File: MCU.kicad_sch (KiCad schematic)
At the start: 17 parts, among them J1 Conn_ARM_SWD_TagConnect_TC203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, U1 MCU_0001, Y1 CLK_0001

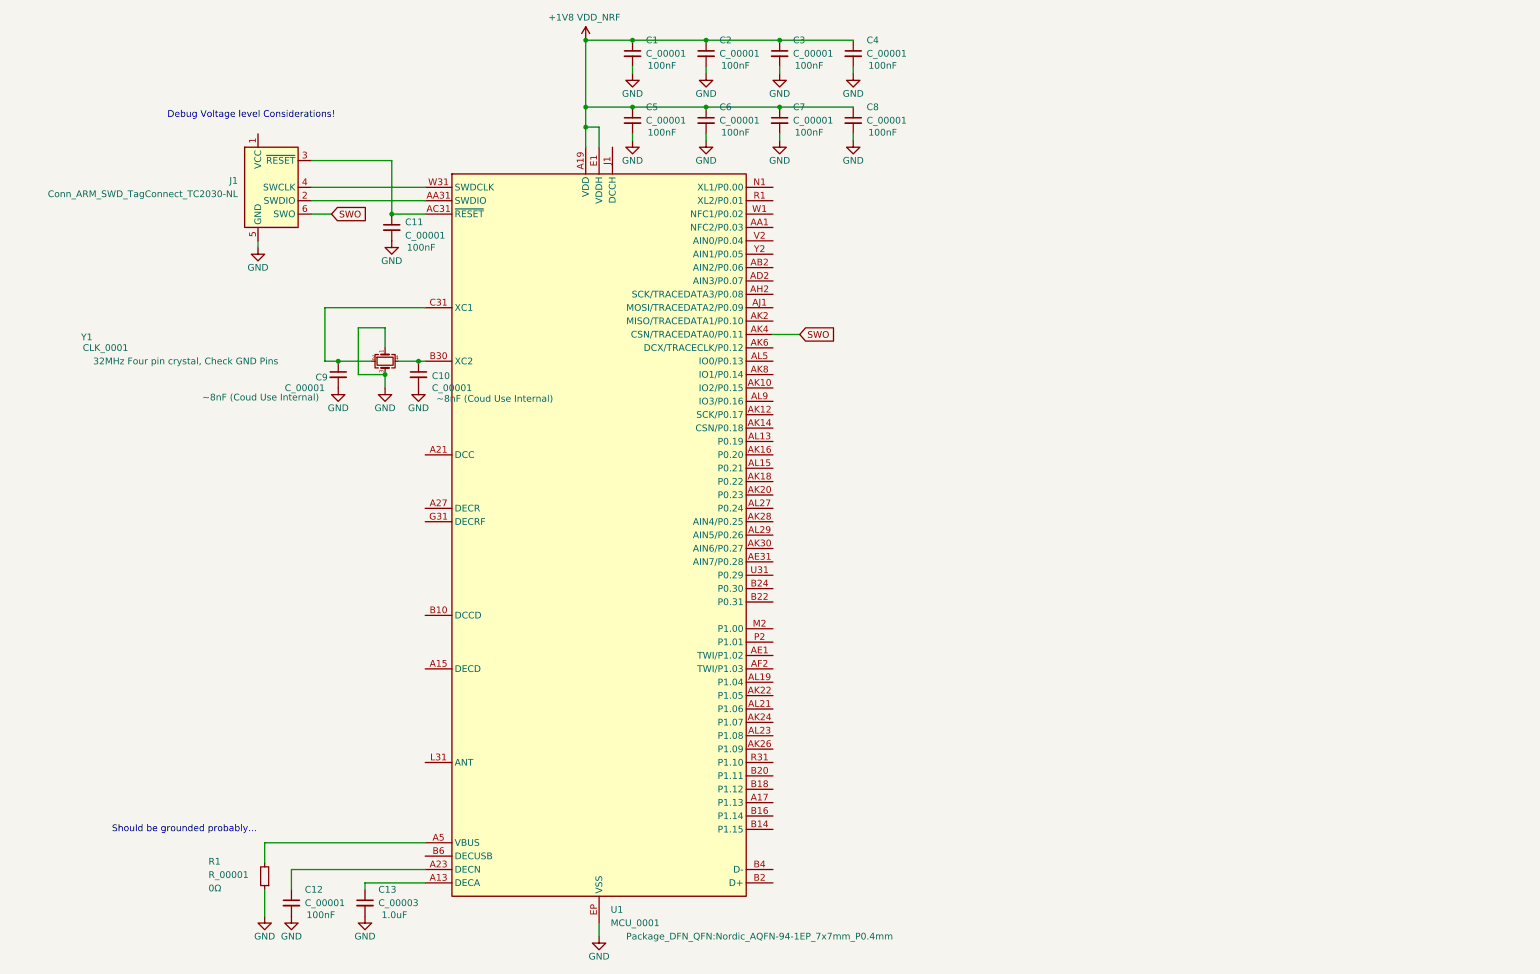
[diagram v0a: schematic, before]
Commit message: added inductors for DCDC regulators
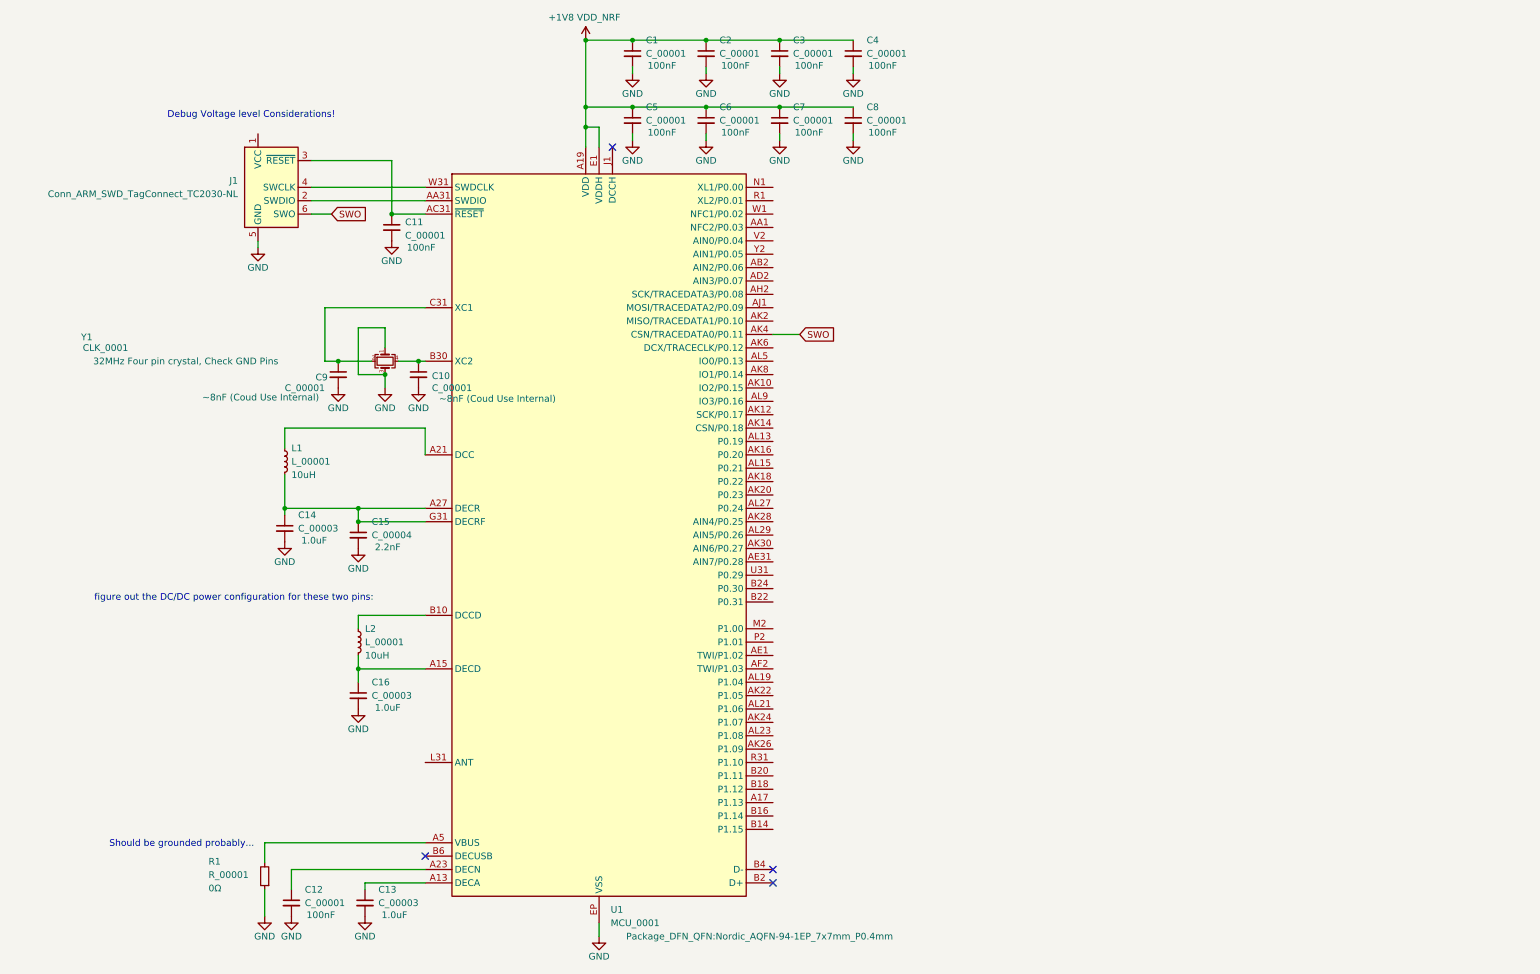
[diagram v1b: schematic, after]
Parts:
- added C14, C16: C_00003, symbol mic_patch_parts:C_00003
- added C15: C_00004, symbol mic_patch_parts:C_00004
- added L1, L2: L_00001, symbol mic_patch_parts:L_00001
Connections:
- net GND: now also C14.2, C15.2, C16.2
- net at U1.A15 (DECD): now also C16.1, L2.2
- net at U1.A21 (DCC): now also L1.1
- net at U1.A27 (DECR): now also U1.G31 (DECRF), C14.1, C15.1, L1.2
- net at U1.B10 (DCCD): now also L2.1
- no-connect marks 0 -> 4
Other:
- note added: "figure out the DC/DC power configuration for these two pins:"

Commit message: routed power
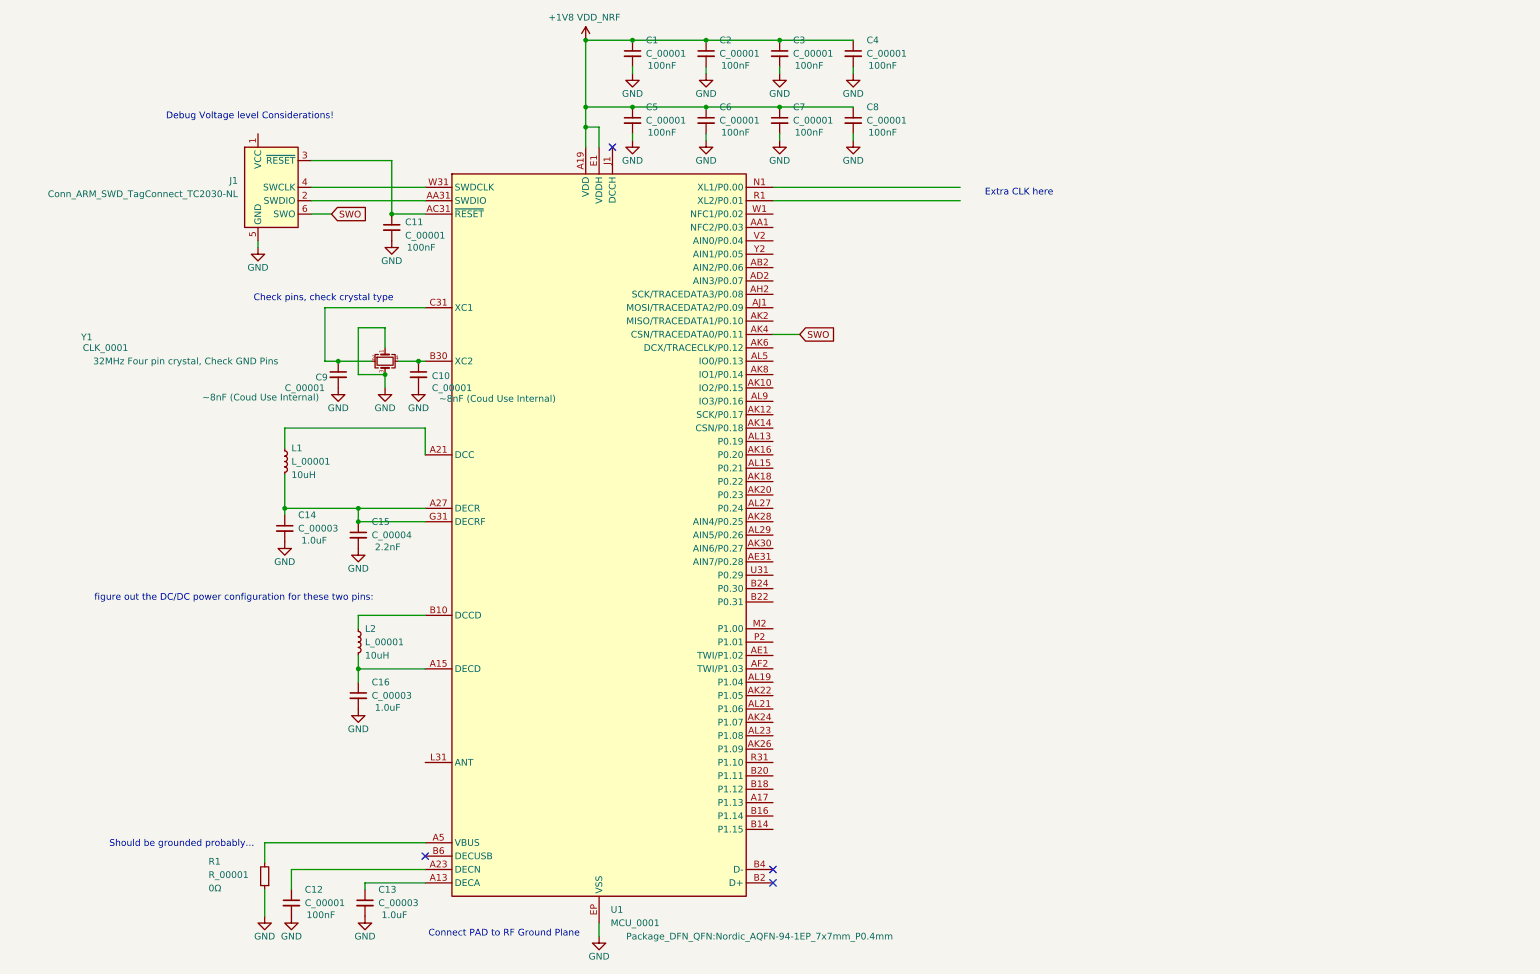
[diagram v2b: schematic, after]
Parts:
- R1: LCSC PNs C11702 -> (none); MPNs 0402WGF1001TCE -> (none)
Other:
- note added: "Check pins, check crystal type"
- note added: "Connect PAD to RF Ground Plane"
- note added: "Extra CLK here"
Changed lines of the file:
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@@
+	(wire
+		(pts
+			(xy 144.78 48.26) (xy 180.34 48.26)
+		)
+		(stroke
+			(width 0)
+			(type default)
+		)
+	)
 	(wire
 		(pts
@@
 	(wire
 		(pts
+			(xy 144.78 50.8) (xy 180.34 50.8)
+		)
+		(stroke
+			(width 0)
+			(type default)
+		)
+	)
+	(wire
+		(pts
 			(xy 66.04 74.93) (xy 71.12 74.93)
 		)
@@
 			(width 0)
 			(type default)
+		)
+	)
+	(text "Extra CLK here"
+		(exclude_from_sim no)
+		(at 191.516 49.276 0)
+		(effects
+			(font
+				(size 1.27 1.27)
+			)
+		)
+	)
+	(text "Connect PAD to RF Ground Plane"
+		(exclude_from_sim no)
+		(at 93.726 189.992 0)
+		(effects
+			(font
+				(size 1.27 1.27)
+			)
 		)
 	)
@@
 		)
 	)
+	(text "Check pins, check crystal type"
+		(exclude_from_sim no)
+		(at 59.436 69.342 0)
+		(effects
+			(font
+				(size 1.27 1.27)
+			)
+		)
+	)
 	(text "Should be grounded probably..."
 		(exclude_from_sim no)
@@
 	(text "Debug Voltage level Considerations!"
 		(exclude_from_sim no)
-		(at 45.72 34.544 0)
+		(at 45.466 34.798 0)
 		(effects
 			(font
@@
 			)
 		)
-		(property "MPNs" "0402WGF1001TCE"
+		(property "MPNs" ""
 			(at 48.26 179.07 0)
 			(effects
@@
 			)
 		)
-		(property "LCSC PNs" "C11702"
+		(property "LCSC PNs" ""
 			(at 48.26 179.07 0)
 			(effects

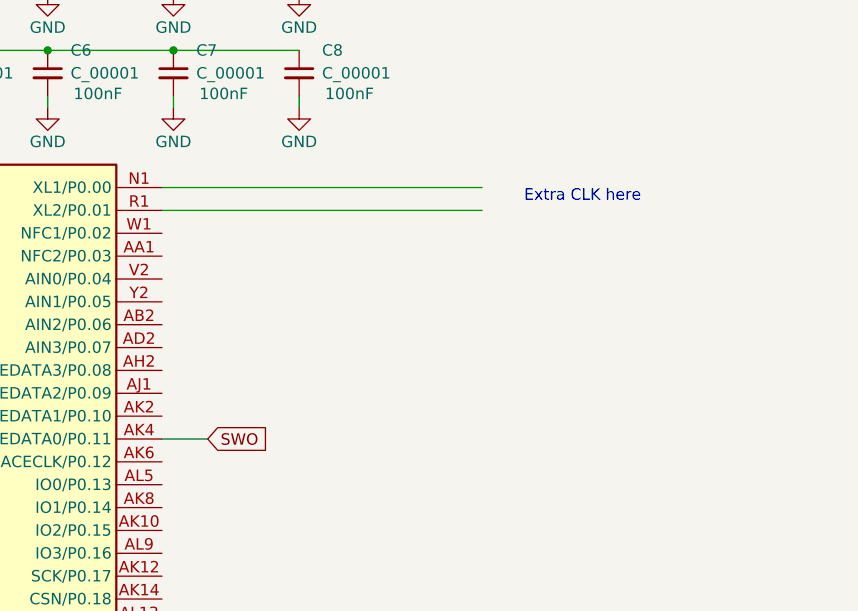
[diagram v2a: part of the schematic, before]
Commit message: added in LFCLK
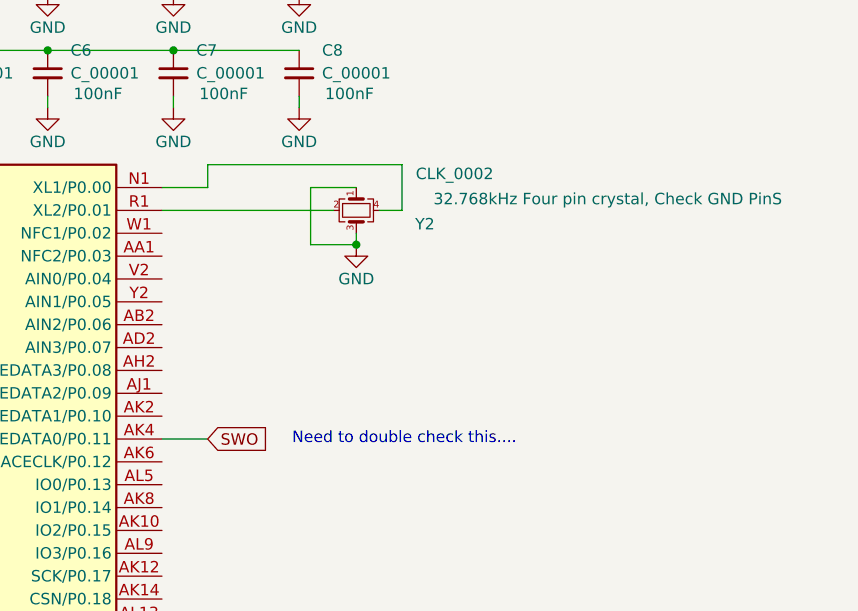
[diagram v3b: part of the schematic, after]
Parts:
- added Y2: CLK_0002, symbol mic_patch_parts:CLK_0002
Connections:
- net GND: now also Y2.1, Y2.3
- net at U1.N1 (XL1/P0.00): now also Y2.4
- net at U1.R1 (XL2/P0.01): now also Y2.2
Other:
- note added: "Need to double check this...."
- note removed: "Extra CLK here"

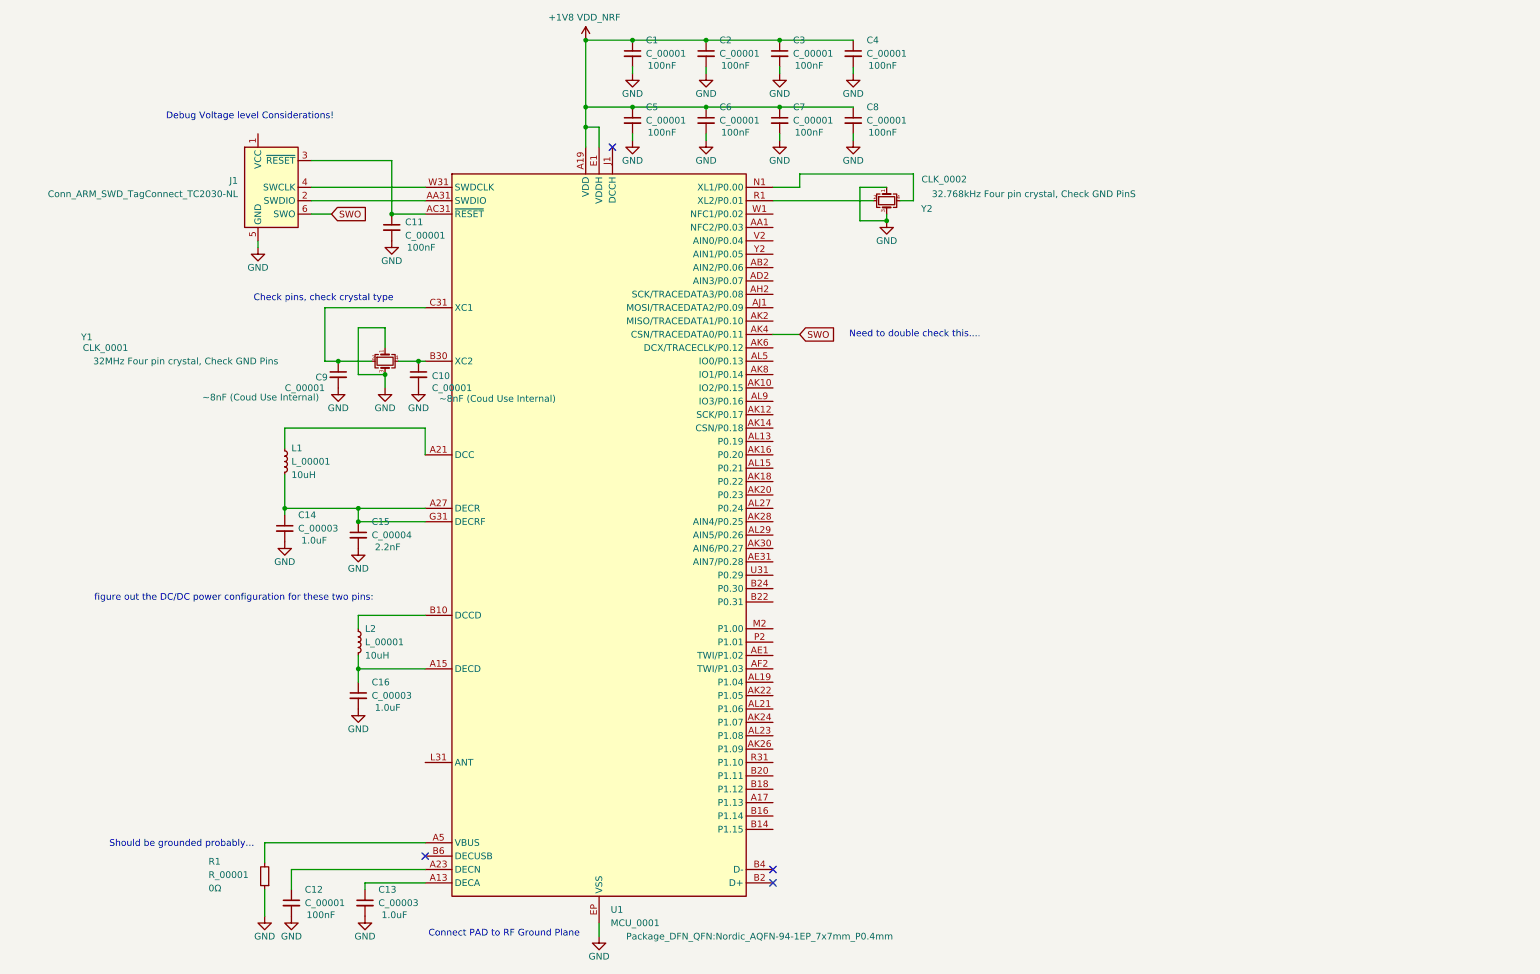
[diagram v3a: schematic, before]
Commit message: added ADAU7002 Symbol
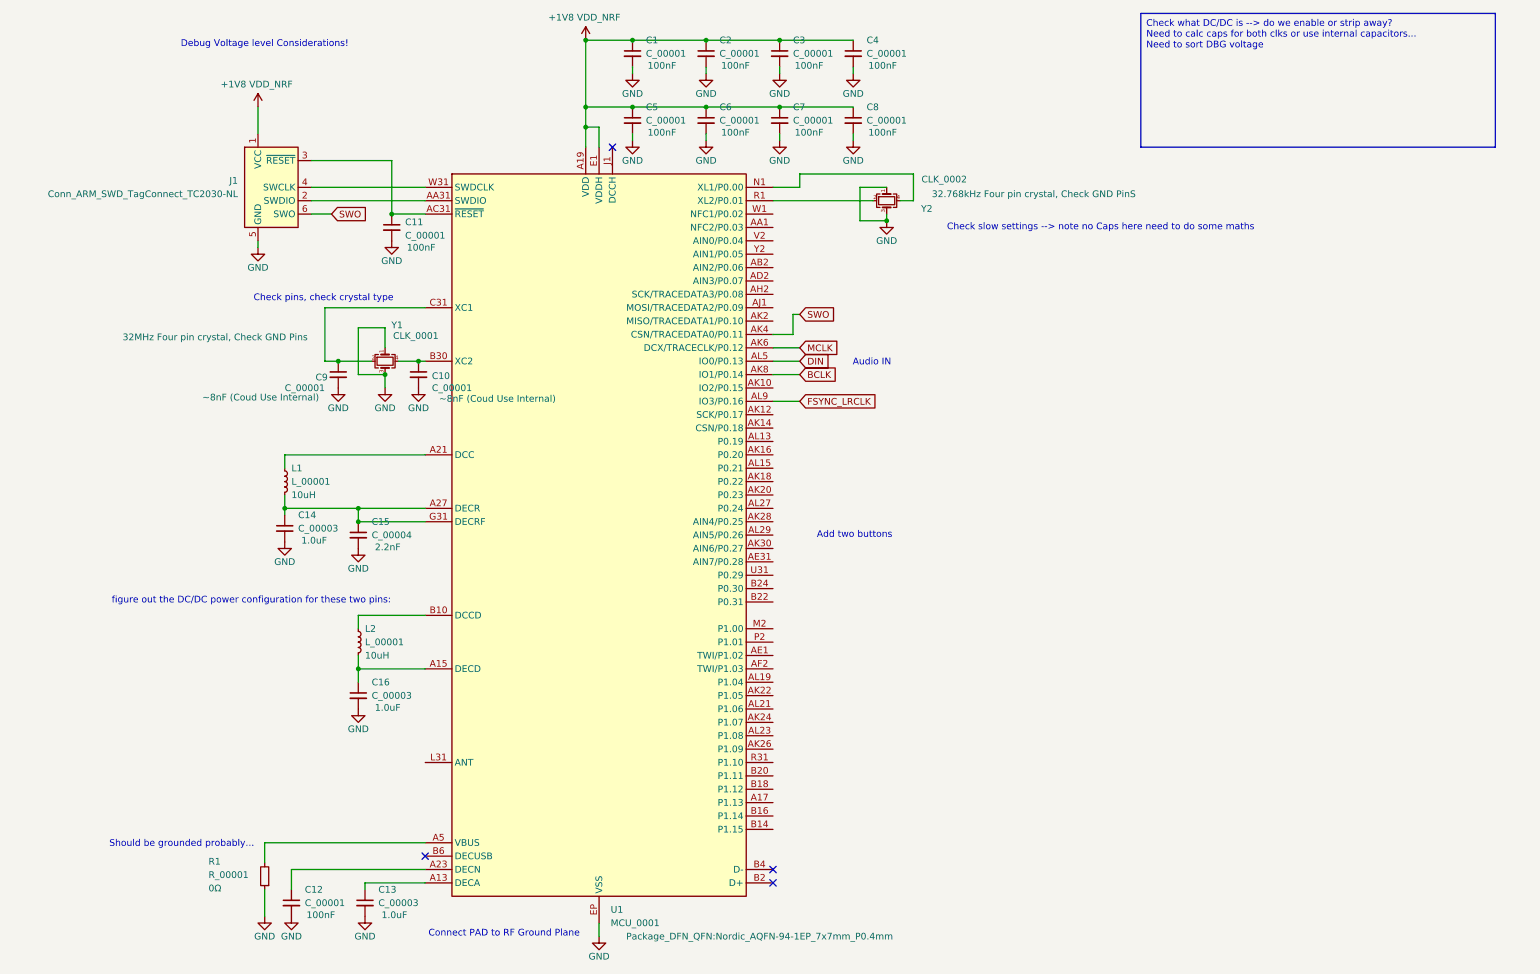
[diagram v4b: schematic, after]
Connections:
- net +1V8 VDD_NRF: now also J1.1 (VCC)
- net MCLK: now reaches U1.AK6 (DCX/TRACECLK/P0.12)
- net BCLK: now reaches U1.AK8 (IO1/P0.14)
- net DIN: now reaches U1.AL5 (IO0/P0.13)
- net FSYNC_LRCLK: now reaches U1.AL9 (IO3/P0.16)
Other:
- note added: "Add two buttons"
- note added: "Audio IN"
- note added: "Check slow settings --> note no Caps here need to do some maths"
- note removed: "Need to double check this...."
- moved on the sheet: L1

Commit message: added MEMS microphone symbol
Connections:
- net MCLK: no longer U1.AK6 (DCX/TRACECLK/P0.12)
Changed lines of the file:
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@@
-	(wire
-		(pts
-			(xy 144.78 78.74) (xy 149.86 78.74)
-		)
-		(stroke
-			(width 0)
-			(type default)
-		)
-	)
 	(wire
 		(pts

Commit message: added rudimentary RF matching network
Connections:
- net RF_ANT: now reaches U1.L31 (ANT)
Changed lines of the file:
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@@
+	(wire
+		(pts
+			(xy 74.93 157.48) (xy 78.74 157.48)
+		)
+		(stroke
+			(width 0)
+			(type default)
+		)
+	)
 	(wire
 		(pts
@@
 		)
 	)
-	(text_box "Check what DC/DC is --> do we enable or strip away?\nNeed to calc caps for both clks or use internal capacitors...\nNeed to sort DBG voltage"
+	(text_box "Check what DC/DC is --> do we enable or strip away?\nNeed to calc caps for both clks or use internal capacitors...\nNeed to sort DBG voltage\nOperating in Single Supply mode"
 		(exclude_from_sim no)
 		(at 214.63 15.24 0)
@@
 	(text "Audio IN"
 		(exclude_from_sim no)
-		(at 163.576 81.534 0)
+		(at 169.418 84.074 0)
 		(effects
 			(font
@@
 		)
 	)
+	(global_label "RF_ANT"
+		(shape input)
+		(at 74.93 157.48 180)
+		(fields_autoplaced yes)
+		(effects
+			(font
+				(size 1.27 1.27)
+			)
+			(justify right)
+		)
+		(property "Intersheetrefs" "${INTERSHEET_REFS}"
+			(at 65.2319 157.48 0)
+			(effects
+				(font
+					(size 1.27 1.27)
+				)
+				(justify right)
+				(hide yes)
+			)
+		)
+	)
 	(global_label "DIN"
 		(shape input)
@@
 			(effects
 				(font
-					(size 1.27 1.27)
-				)
-				(justify left)
-				(hide yes)
-			)
-		)
-	)
-	(global_label "MCLK"
-		(shape input)
-		(at 149.86 78.74 0)
-		(fields_autoplaced yes)
-		(effects
-			(font
-				(size 1.27 1.27)
-			)
-			(justify left)
-		)
-		(property "Intersheetrefs" "${INTERSHEET_REFS}"
-			(at 157.8647 78.74 0)
-			(effects
-				(font
